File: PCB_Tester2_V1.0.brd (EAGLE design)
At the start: 99.1 x 99.1 mm, 60 parts, among them IC1 74HC595N, IC2 74HC165N, J1 DCJ0202, K1 G5L, K2 G5L, K3 G5L, K4 G5L, T1 2N2222, T2 2N2222, T3 2N2222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

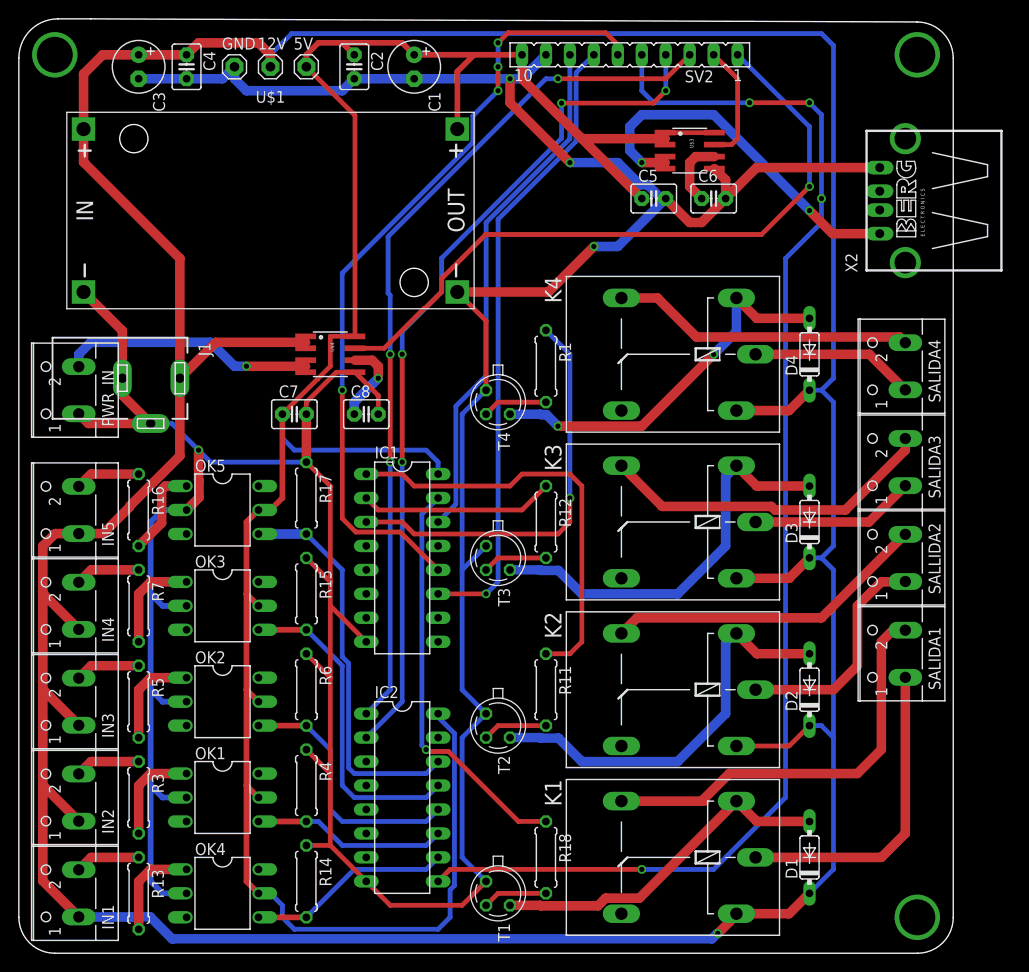
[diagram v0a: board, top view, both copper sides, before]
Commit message: V1.0
Máscara agregada
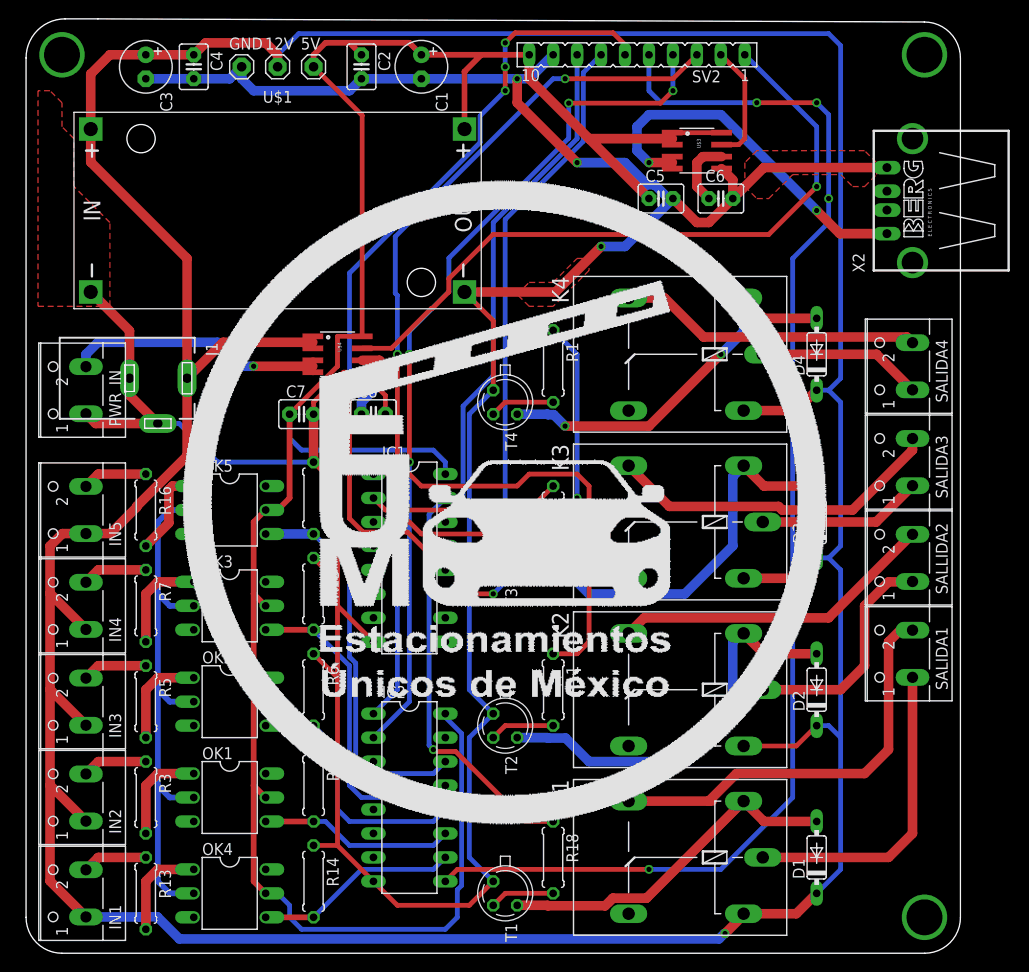
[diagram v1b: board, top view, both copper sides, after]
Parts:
- moved 5V 0.76 mm to (31.2, 94.0)
- moved C1 0.76 mm to (42.7, 94.0)
- moved C2 0.76 mm to (36.3, 94.0)
- moved C3 0.76 mm to (13.5, 94.0)
- moved C4 0.76 mm to (18.5, 94.0)
- moved C5 0.76 mm to (68.1, 80.0)
- moved C6 0.76 mm to (74.4, 80.0)
- moved C7 0.76 mm to (30.0, 57.1)
- moved C8 0.76 mm to (37.6, 57.1)
- moved D1 0.76 mm to (84.6, 10.2)
- moved D2 0.76 mm to (84.6, 27.9)
- moved D3 0.76 mm to (84.6, 45.7)
- moved D4 0.76 mm to (84.6, 63.5)
- moved GND 0.76 mm to (23.6, 94.0)
- moved IC1 0.76 mm to (41.4, 41.9)
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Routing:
- added copper zone on layer 1, net GND
